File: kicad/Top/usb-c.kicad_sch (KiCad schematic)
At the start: 11 parts

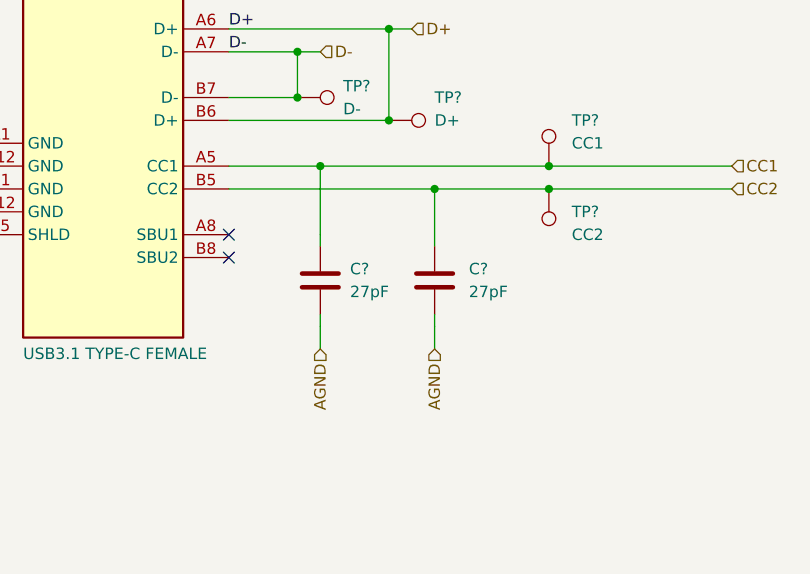
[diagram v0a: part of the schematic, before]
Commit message: Updated USB-C sheet to include SBU1 and 2
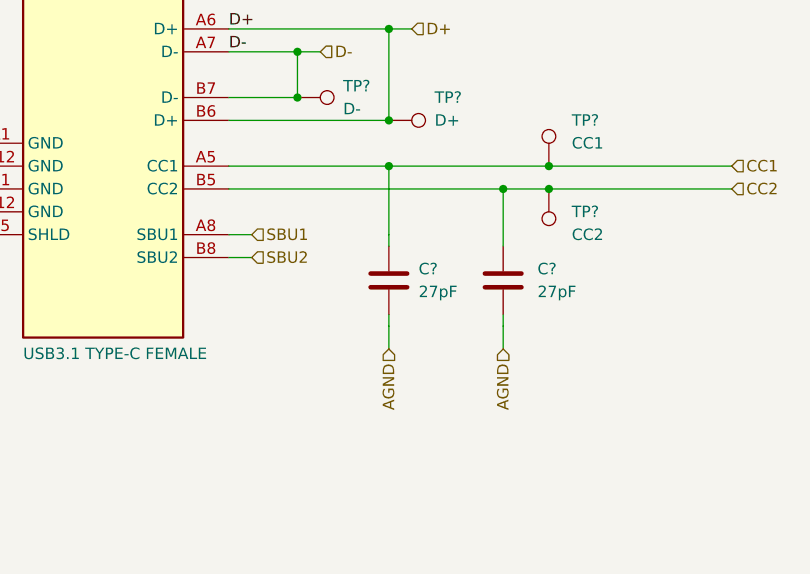
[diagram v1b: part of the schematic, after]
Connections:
- net SBU1: now reaches J?.A8 (SBU1)
- net SBU2: now reaches J?.B8 (SBU2)
- no-connect marks 10 -> 8
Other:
- moved on the sheet: C?
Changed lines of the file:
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@@
   (junction (at 109.22 129.54) (diameter 0) (color 0 0 0 0)
   )
-  (junction (at 162.56 132.08) (diameter 0) (color 0 0 0 0)
+  (junction (at 170.18 132.08) (diameter 0) (color 0 0 0 0)
   )
   (junction (at 175.26 129.54) (diameter 0) (color 0 0 0 0)
   )
-  (junction (at 149.86 129.54) (diameter 0) (color 0 0 0 0)
+  (junction (at 157.48 129.54) (diameter 0) (color 0 0 0 0)
   )
   (junction (at 149.86 88.9) (diameter 0) (color 0 0 0 0)
@@
   (no_connect (at 139.7 86.36))
   (no_connect (at 139.7 106.68))
-  (no_connect (at 139.7 139.7))
-  (no_connect (at 139.7 137.16))
-  (wire (pts (xy 149.86 146.05) (xy 149.86 147.32))
+  (wire (pts (xy 157.48 146.05) (xy 157.48 147.32))
     (stroke (width 0) (type default) (color 0 0 0 0))
   )
@@
     (stroke (width 0.254) (type default) (color 0 0 0 0))
   )
-  (wire (pts (xy 139.7 129.54) (xy 149.86 129.54))
+  (wire (pts (xy 139.7 129.54) (xy 157.48 129.54))
     (stroke (width 0.254) (type default) (color 0 0 0 0))
   )
@@
     (stroke (width 0.254) (type default) (color 0 0 0 0))
   )
-  (wire (pts (xy 162.56 146.05) (xy 162.56 147.32))
-    (stroke (width 0) (type default) (color 0 0 0 0))
-  )
-  (wire (pts (xy 162.56 132.08) (xy 162.56 138.43))
+  (wire (pts (xy 170.18 146.05) (xy 170.18 147.32))
+    (stroke (width 0) (type default) (color 0 0 0 0))
+  )
+  (wire (pts (xy 170.18 132.08) (xy 170.18 138.43))
     (stroke (width 0) (type default) (color 0 0 0 0))
   )
@@
     (stroke (width 0) (type default) (color 0 0 0 0))
   )
-  (wire (pts (xy 149.86 137.16) (xy 149.86 138.43))
+  (wire (pts (xy 157.48 137.16) (xy 157.48 138.43))
     (stroke (width 0) (type default) (color 0 0 0 0))
   )
@@
     (stroke (width 0.254) (type default) (color 0 0 0 0))
   )
-  (wire (pts (xy 162.56 132.08) (xy 175.26 132.08))
+  (wire (pts (xy 170.18 132.08) (xy 175.26 132.08))
     (stroke (width 0) (type default) (color 0 0 0 0))
   )
@@
     (stroke (width 0) (type default) (color 0 0 0 0))
   )
-  (wire (pts (xy 139.7 132.08) (xy 162.56 132.08))
+  (wire (pts (xy 139.7 132.08) (xy 170.18 132.08))
     (stroke (width 0.254) (type default) (color 0 0 0 0))
   )
@@
     (stroke (width 0.254) (type default) (color 0 0 0 0))
   )
+  (wire (pts (xy 139.7 139.7) (xy 142.24 139.7))
+    (stroke (width 0) (type default) (color 0 0 0 0))
+  )
   (wire (pts (xy 139.7 73.66) (xy 144.78 73.66))
     (stroke (width 0.254) (type default) (color 0 0 0 0))
@@
     (stroke (width 0.254) (type default) (color 0 0 0 0))
   )
-  (wire (pts (xy 162.56 149.86) (xy 162.56 147.32))
-    (stroke (width 0.254) (type default) (color 0 0 0 0))
-  )
-  (wire (pts (xy 149.86 137.16) (xy 149.86 129.54))
+  (wire (pts (xy 170.18 149.86) (xy 170.18 147.32))
+    (stroke (width 0.254) (type default) (color 0 0 0 0))
+  )
+  (wire (pts (xy 157.48 137.16) (xy 157.48 129.54))
     (stroke (width 0.254) (type default) (color 0 0 0 0))
   )
@@
     (stroke (width 0.254) (type default) (color 0 0 0 0))
   )
-  (wire (pts (xy 149.86 129.54) (xy 175.26 129.54))
+  (wire (pts (xy 139.7 137.16) (xy 142.24 137.16))
+    (stroke (width 0) (type default) (color 0 0 0 0))
+  )
+  (wire (pts (xy 157.48 129.54) (xy 175.26 129.54))
     (stroke (width 0.254) (type default) (color 0 0 0 0))
   )
@@
     (stroke (width 0) (type default) (color 0 0 0 0))
   )
-  (wire (pts (xy 149.86 149.86) (xy 149.86 147.32))
+  (wire (pts (xy 157.48 149.86) (xy 157.48 147.32))
     (stroke (width 0.254) (type default) (color 0 0 0 0))
   )
@@
     (effects (font (size 1.27 1.27)) (justify left bottom))
   )
-  (hierarchical_label "AGND" (shape input) (at 162.56 149.86 270)
+  (hierarchical_label "AGND" (shape input) (at 170.18 149.86 270)
     (effects (font (size 1.27 1.27)) (justify right))
   )
-  (hierarchical_label "AGND" (shape input) (at 149.86 149.86 270)
+  (hierarchical_label "AGND" (shape input) (at 157.48 149.86 270)
     (effects (font (size 1.27 1.27)) (justify right))
   )
@@
     (effects (font (size 1.27 1.27)) (justify left))
   )
+  (hierarchical_label "SBU2" (shape input) (at 142.24 139.7 0)
+    (effects (font (size 1.27 1.27)) (justify left))
+  )
   (hierarchical_label "D-" (shape input) (at 149.86 116.84 0)
     (effects (font (size 1.27 1.27)) (justify left))
@@
   )
   (hierarchical_label "D+" (shape input) (at 160.02 114.3 0)
+    (effects (font (size 1.27 1.27)) (justify left))
+  )
+  (hierarchical_label "SBU1" (shape input) (at 142.24 137.16 0)
     (effects (font (size 1.27 1.27)) (justify left))
   )
@@
     (pin "1")
   )
-  (symbol (lib_id "Device:C") (at 162.56 142.24 0) (unit 1)
+  (symbol (lib_id "Device:C") (at 170.18 142.24 0) (unit 1)
     (in_bom yes) (on_board yes) (fields_autoplaced)
-    (property "Reference" "C?" (id 0) (at 166.37 140.9699 0)
-      (effects (font (size 1.27 1.27)) (justify left))
-    )
-    (property "Value" "27pF" (id 1) (at 166.37 143.5099 0)
-      (effects (font (size 1.27 1.27)) (justify left))
-    )
-    (property "Footprint" "" (id 2) (at 163.5252 146.05 0)
-      (effects (font (size 1.27 1.27)) hide)
-    )
-    (property "Datasheet" "~" (id 3) (at 162.56 142.24 0)
-      (effects (font (size 1.27 1.27)) hide)
-    )
-    (property "Description" "50V" (id 4) (at 162.56 142.24 0)
+    (property "Reference" "C?" (id 0) (at 173.99 140.9699 0)
+      (effects (font (size 1.27 1.27)) (justify left))
+    )
+    (property "Value" "27pF" (id 1) (at 173.99 143.5099 0)
+      (effects (font (size 1.27 1.27)) (justify left))
+    )
+    (property "Footprint" "" (id 2) (at 171.1452 146.05 0)
+      (effects (font (size 1.27 1.27)) hide)
+    )
+    (property "Datasheet" "~" (id 3) (at 170.18 142.24 0)
+      (effects (font (size 1.27 1.27)) hide)
+    )
+    (property "Description" "50V" (id 4) (at 170.18 142.24 0)
       (effects (font (size 1.27 1.27)) hide)
     )
@@
     (pin "1")
   )
-  (symbol (lib_id "Device:C") (at 149.86 142.24 0) (unit 1)
-    (in_bom yes) (on_board yes)
-    (property "Reference" "C?" (id 0) (at 153.162 140.97 0)
-      (effects (font (size 1.27 1.27)) (justify left))
-    )
-    (property "Value" "27pF" (id 1) (at 153.162 143.51 0)
-      (effects (font (size 1.27 1.27)) (justify left))
-    )
-    (property "Footprint" "" (id 2) (at 150.8252 146.05 0)
-      (effects (font (size 1.27 1.27)) hide)
-    )
-    (property "Datasheet" "~" (id 3) (at 149.86 142.24 0)
-      (effects (font (size 1.27 1.27)) hide)
-    )
-    (property "Description" "50V" (id 4) (at 149.86 142.24 0)
-      (effects (font (size 1.27 1.27)) hide)
-    )
+  (symbol (lib_id "Device:C") (at 157.48 142.24 0) (unit 1)
+    (in_bom yes) (on_board yes)
+    (property "Reference" "C?" (id 0) (at 160.782 140.97 0)
+      (effects (font (size 1.27 1.27)) (justify left))
+    )
+    (property "Value" "27pF" (id 1) (at 160.782 143.51 0)
+      (effects (font (size 1.27 1.27)) (justify left))
+    )
+    (property "Footprint" "" (id 2) (at 158.4452 146.05 0)
+      (effects (font (size 1.27 1.27)) hide)
+    )
+    (property "Datasheet" "~" (id 3) (at 157.48 142.24 0)
+      (effects (font (size 1.27 1.27)) hide)
+    )
+    (property "Description" "50V" (id 4) (at 157.48 142.24 0)
+      (effects (font (size 1.27 1.27)) hide)
+    )
